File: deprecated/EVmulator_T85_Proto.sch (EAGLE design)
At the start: 24 parts, among them Q2 5.8A/30V/35mΩ, U1 ATTINY85V

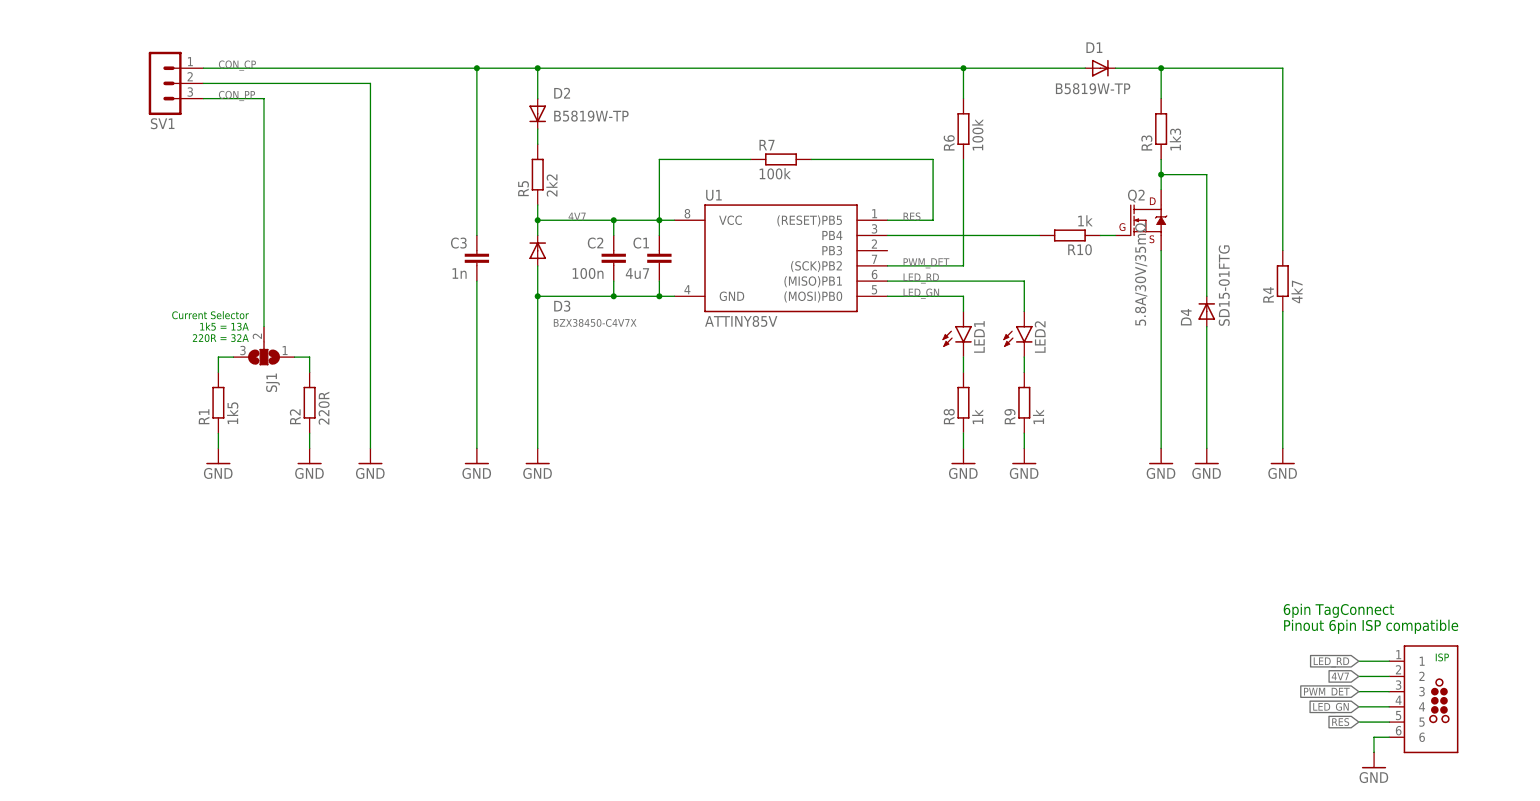
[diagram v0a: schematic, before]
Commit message: * moved prototype board to deprecated (will not be maintained in the future= * added connection drawing to schematic, updated output
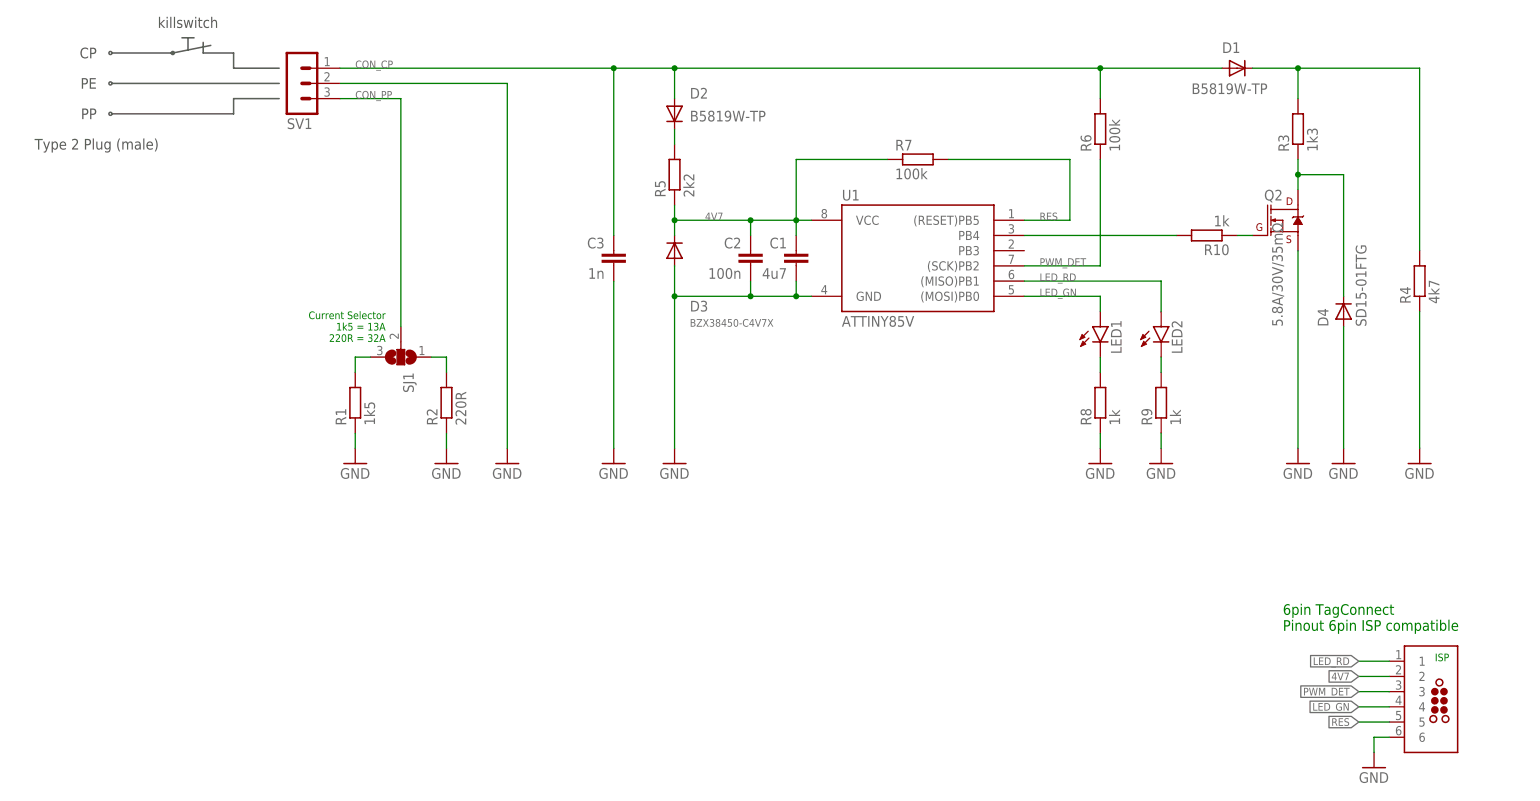
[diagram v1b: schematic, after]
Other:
- note added: "CP"
- note added: "PE"
- note added: "PP"
- note added: "Type 2 Plug (male)"
- note added: "killswitch"
- moved on the sheet: C1, C2, C3, D1, D2, D3, D4, LED1, LED2, Q2, R1, R10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
